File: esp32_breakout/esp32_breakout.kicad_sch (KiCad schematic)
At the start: 25 parts, among them J1 JST B5B-PH-K-S, J10 JST B6B-PH-K-S, J2 JST B5B-PH-K-S, J3 JST B7B-PH-K-S, J4 XT30U-M, J5 HDR M VERT 12p 2.54mm, J9 JST B6B-PH-K-S, SW1 SS12D10, U1 ESP32 DEV KIT Module 30-pin, U2 LM2596 Module

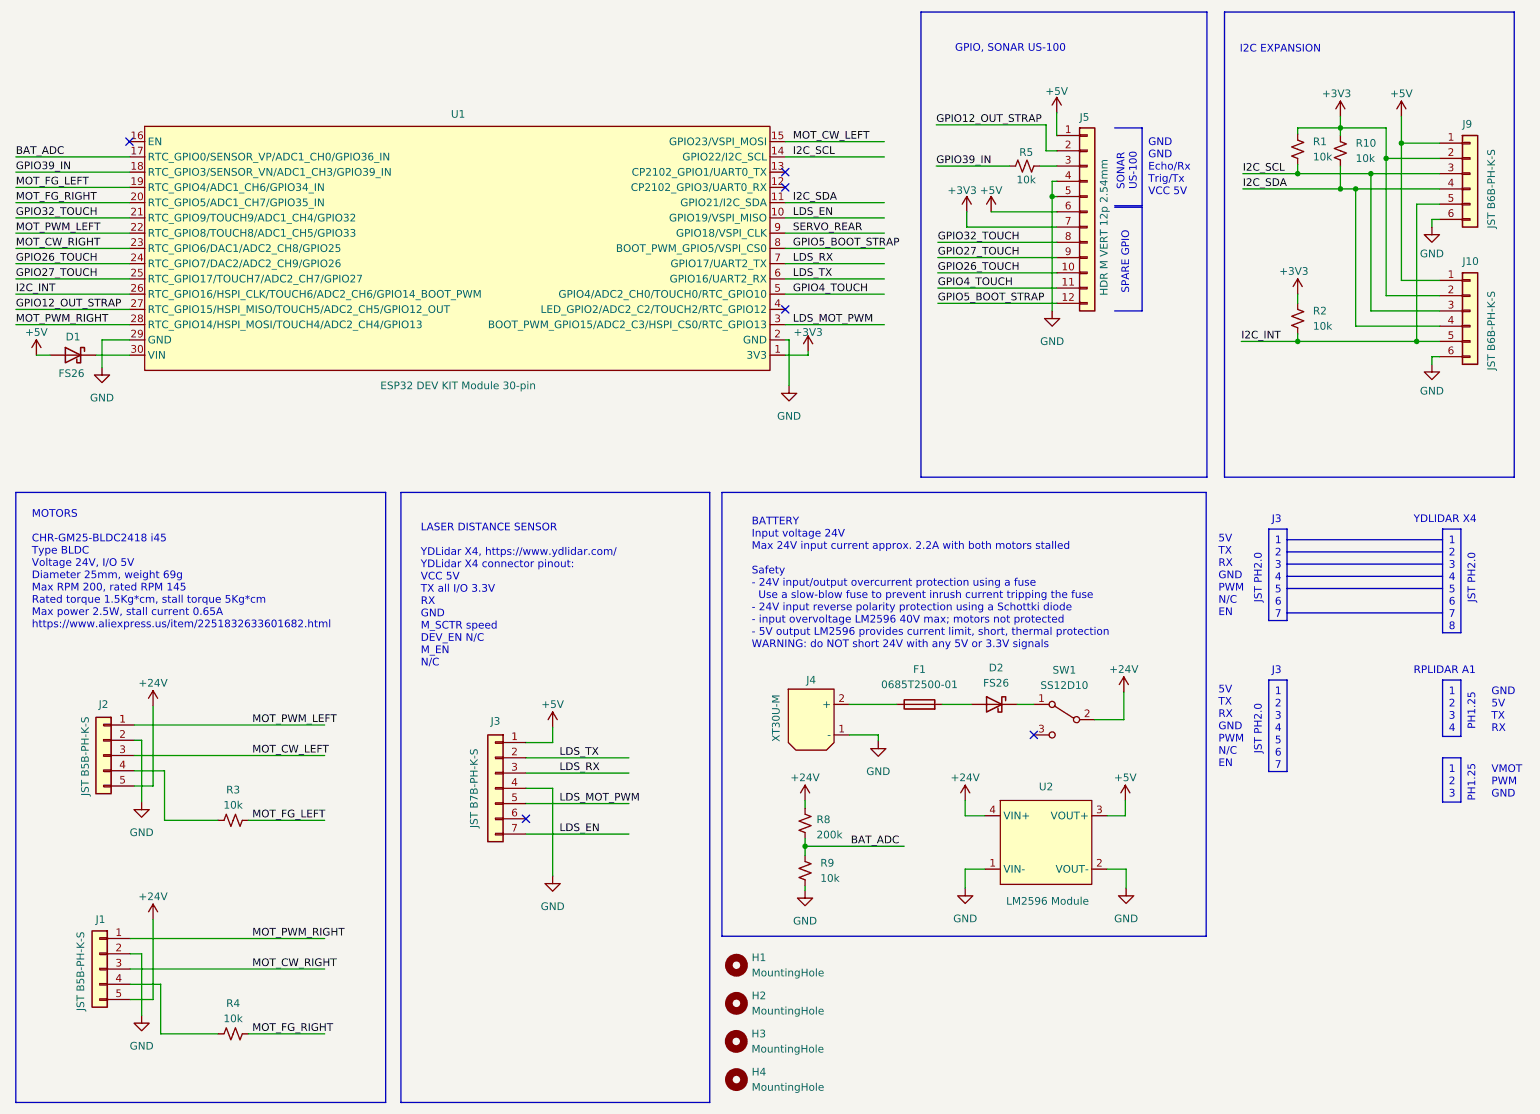
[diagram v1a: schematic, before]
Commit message: ZH extension connector; 6-pin LDS connector
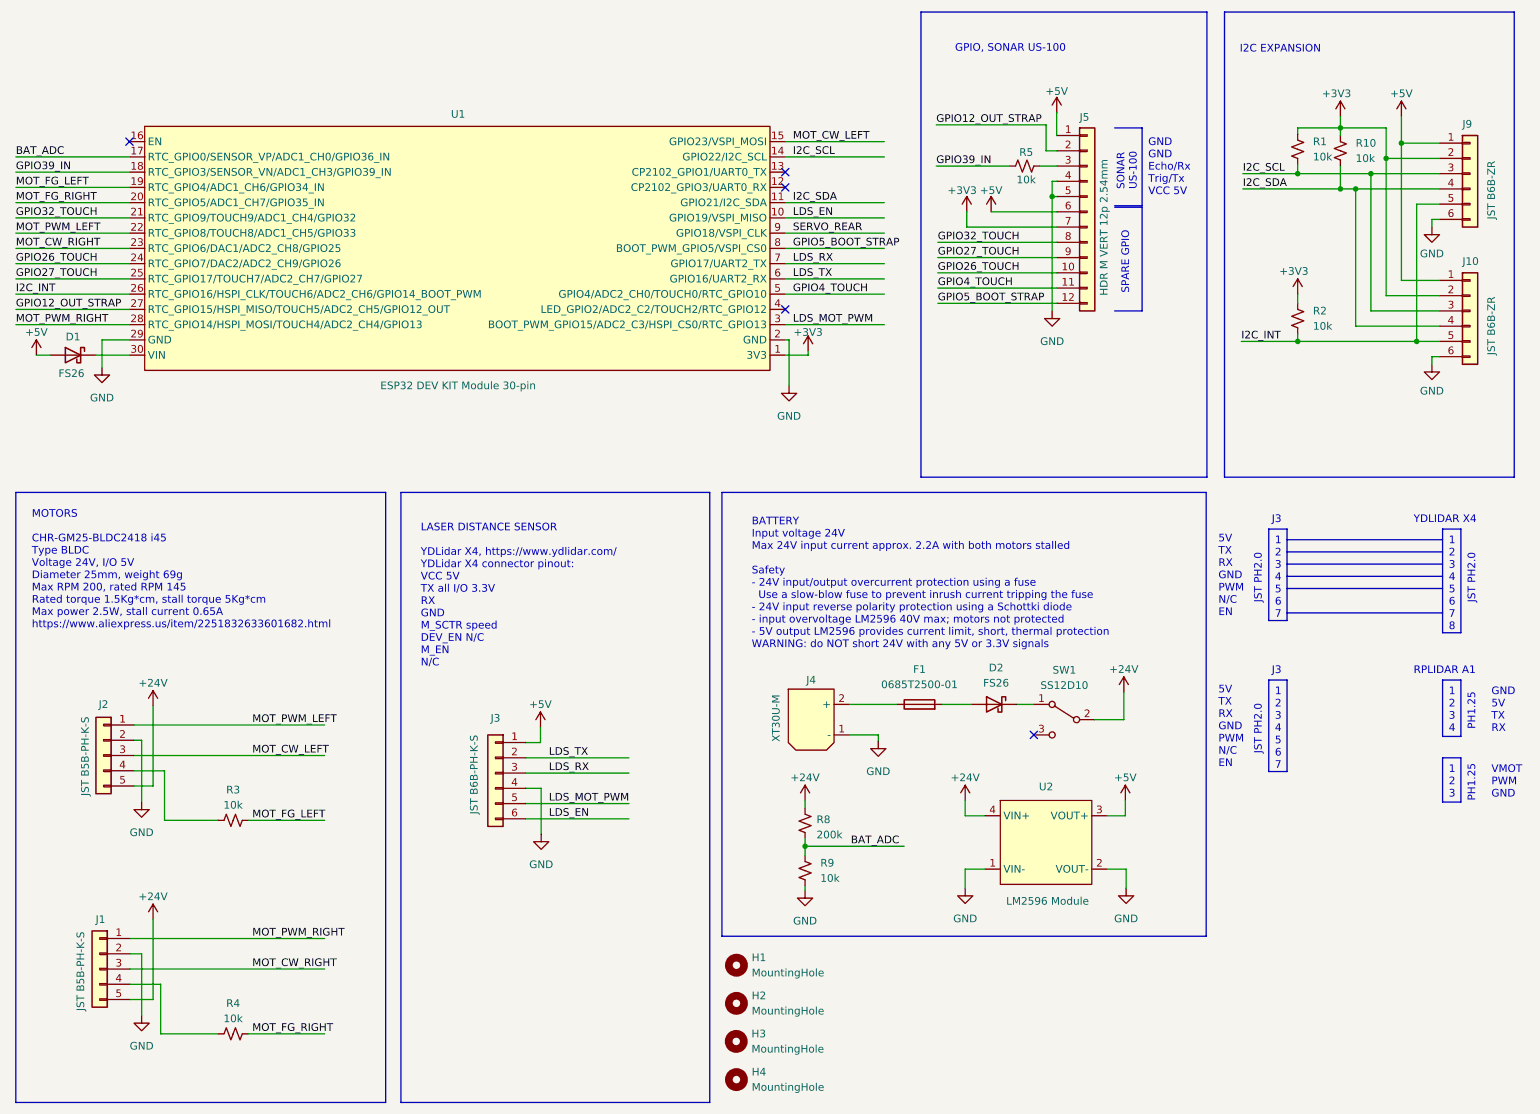
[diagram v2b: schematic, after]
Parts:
- removed J3: JST B7B-PH-K-S, Connector_JST:JST_PH_B7B-PH-K_1x07_P2.00mm_Vertical, symbol Connector_Generic:Conn_01x07
- added J3: JST B6B-PH-K-S, Connector_JST:JST_PH_B6B-PH-K_1x06_P2.00mm_Vertical, symbol Connector_Generic:Conn_01x06
- J10, J9: value JST B6B-PH-K-S -> JST B6B-ZR; footprint Connector_JST:JST_PH_B6B-PH-K_1x06_P2.00mm_Vertical -> Makerspet:JST_ZH_B6B-ZR_1x06_P1.50mm_Vertical
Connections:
- net +5V: now also J3.1 (Pin_1)
- net GND: now also J3.4 (Pin_4)
- net LDS_EN: now also J3.6 (Pin_6)
- net LDS_MOT_PWM: now also J3.5 (Pin_5)
- net LDS_RX: now also J3.3 (Pin_3)
- net LDS_TX: now also J3.2 (Pin_2)
- no-connect marks 6 -> 5
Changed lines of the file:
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@@
   (title_block
     (title "Maker's Pet ESP32 Breakout")
-    (date "2023-12-29")
-    (rev "1.1.0")
+    (date "2024-03-06")
+    (rev "1.2.0")
     (company "Maker's Pet")
     (comment 1 "makerspet.com")
@@
   (no_connect (at 142.748 44.45))
   (no_connect (at 142.748 41.91))
-  (no_connect (at 99.568 149.606))
   (no_connect (at 142.748 64.77))
   (no_connect (at 184.15 135.636))
@@
     (stroke (width 0) (type default))
   )
-  (wire (pts (xy 99.568 136.906) (xy 104.013 136.906))
+  (wire (pts (xy 99.568 136.906) (xy 101.981 136.906))
     (stroke (width 0) (type default))
   )
@@
     (stroke (width 0) (type default))
   )
-  (wire (pts (xy 104.013 134.366) (xy 104.013 136.906))
+  (wire (pts (xy 101.981 134.366) (xy 101.981 136.906))
     (stroke (width 0) (type default))
   )
@@
     (stroke (width 0) (type default))
   )
+  (wire (pts (xy 99.568 149.606) (xy 116.713 149.606))
+    (stroke (width 0) (type default))
+  )
   (wire (pts (xy 14.605 39.37) (xy 33.528 39.37))
     (stroke (width 0) (type default))
@@
     (stroke (width 0) (type default))
   )
-  (wire (pts (xy 99.568 144.526) (xy 104.013 144.526))
+  (wire (pts (xy 99.568 144.526) (xy 102.108 144.526))
     (stroke (width 0) (type default))
   )
@@
     (stroke (width 0) (type default))
   )
-  (wire (pts (xy 104.013 144.526) (xy 104.013 159.131))
+  (wire (pts (xy 102.108 144.526) (xy 102.108 152.146))
     (stroke (width 0) (type default))
   )
@@
   )
   (wire (pts (xy 153.416 130.556) (xy 161.29 130.556))
-    (stroke (width 0) (type default))
-  )
-  (wire (pts (xy 99.568 152.146) (xy 116.713 152.146))
     (stroke (width 0) (type default))
   )
@@
     (effects (font (size 1.27 1.27)) (justify left bottom))
   )
-  (label "LDS_TX" (at 105.156 139.446 0) (fields_autoplaced)
+  (label "LDS_EN" (at 103.378 149.606 0) (fields_autoplaced)
+    (effects (font (size 1.27 1.27)) (justify left bottom))
+  )
+  (label "LDS_TX" (at 103.378 139.446 0) (fields_autoplaced)
     (effects (font (size 1.27 1.27)) (justify left bottom))
   )
@@
     (effects (font (size 1.27 1.27)) (justify left bottom))
   )
-  (label "LDS_MOT_PWM" (at 105.156 147.066 0) (fields_autoplaced)
+  (label "LDS_MOT_PWM" (at 103.378 147.066 0) (fields_autoplaced)
     (effects (font (size 1.27 1.27)) (justify left bottom))
   )
@@
     (effects (font (size 1.27 1.27)) (justify left bottom))
   )
-  (label "LDS_RX" (at 105.156 141.986 0) (fields_autoplaced)
+  (label "LDS_RX" (at 103.378 141.986 0) (fields_autoplaced)
     (effects (font (size 1.27 1.27)) (justify left bottom))
   )
@@
   )
   (label "MOT_PWM_RIGHT" (at 14.605 67.31 0) (fields_autoplaced)
-    (effects (font (size 1.27 1.27)) (justify left bottom))
-  )
-  (label "LDS_EN" (at 105.156 152.146 0) (fields_autoplaced)
     (effects (font (size 1.27 1.27)) (justify left bottom))
   )
@@
       (effects (font (size 1.27 1.27)) (justify left))
     )
-    (property "Value" "JST B6B-PH-K-S" (at 260.35 74.93 90)
+    (property "Value" "JST B6B-ZR" (at 260.35 72.39 90)
       (effects (font (size 1.27 1.27)) (justify left))
     )
-    (property "Footprint" "Connector_JST:JST_PH_B6B-PH-K_1x06_P2.00mm_Vertical" (at 256.794 65.024 0)
+    (property "Footprint" "Makerspet:JST_ZH_B6B-ZR_1x06_P1.50mm_Vertical" (at 256.794 65.024 0)
       (effects (font (size 1.27 1.27)) hide)
     )
@@
         (path "/e24ae185-8f18-408c-aee8-f727519bade3"
           (reference "R1") (unit 1)
-        )
-      )
-    )
-  )
-  (symbol (lib_id "Connector_Generic:Conn_01x07") (at 94.488 144.526 0) (mirror y) (unit 1)
-    (in_bom yes) (on_board yes) (dnp no)
-    (property "Reference" "J3" (at 94.488 133.35 0)
-      (effects (font (size 1.27 1.27)))
-    )
-    (property "Value" "JST B7B-PH-K-S" (at 90.932 144.526 90)
-      (effects (font (size 1.27 1.27)))
-    )
-    (property "Footprint" "Connector_JST:JST_PH_B7B-PH-K_1x07_P2.00mm_Vertical" (at 94.488 144.526 0)
-      (effects (font (size 1.27 1.27)) hide)
-    )
-    (property "Datasheet" "~" (at 94.488 144.526 0)
-      (effects (font (size 1.27 1.27)) hide)
-    )
-    (pin "1")
-    (pin "2")
-    (pin "3")
-    (pin "4")
-    (pin "5")
-    (pin "6")
-    (pin "7")
-    (instances
-      (project "esp32_breakout"
-        (path "/e24ae185-8f18-408c-aee8-f727519bade3"
-          (reference "J3") (unit 1)
         )
       )
@@
     )
   )
-  (symbol (lib_id "power:+5V") (at 104.013 134.366 0) (unit 1)
-    (in_bom yes) (on_board yes) (dnp no) (fields_autoplaced)
-    (property "Reference" "#PWR09" (at 104.013 138.176 0)
-      (effects (font (size 1.27 1.27)) hide)
-    )
-    (property "Value" "+5V" (at 104.013 130.556 0)
-      (effects (font (size 1.27 1.27)))
-    )
-    (property "Footprint" "" (at 104.013 134.366 0)
-      (effects (font (size 1.27 1.27)) hide)
-    )
-    (property "Datasheet" "" (at 104.013 134.366 0)
+  (symbol (lib_id "power:+5V") (at 101.981 134.366 0) (unit 1)
+    (in_bom yes) (on_board yes) (dnp no) (fields_autoplaced)
+    (property "Reference" "#PWR09" (at 101.981 138.176 0)
+      (effects (font (size 1.27 1.27)) hide)
+    )
+    (property "Value" "+5V" (at 101.981 130.556 0)
+      (effects (font (size 1.27 1.27)))
+    )
+    (property "Footprint" "" (at 101.981 134.366 0)
+      (effects (font (size 1.27 1.27)) hide)
+    )
+    (property "Datasheet" "" (at 101.981 134.366 0)
       (effects (font (size 1.27 1.27)) hide)
     )
@@
     )
   )
-  (symbol (lib_id "power:GND") (at 104.013 159.131 0) (unit 1)
-    (in_bom yes) (on_board yes) (dnp no) (fields_autoplaced)
-    (property "Reference" "#PWR010" (at 104.013 165.481 0)
-      (effects (font (size 1.27 1.27)) hide)
-    )
-    (property "Value" "GND" (at 104.013 164.211 0)
-      (effects (font (size 1.27 1.27)))
-    )
-    (property "Footprint" "" (at 104.013 159.131 0)
-      (effects (font (size 1.27 1.27)) hide)
-    )
-    (property "Datasheet" "" (at 104.013 159.131 0)
+  (symbol (lib_id "power:GND") (at 102.108 152.146 0) (unit 1)
+    (in_bom yes) (on_board yes) (dnp no) (fields_autoplaced)
+    (property "Reference" "#PWR010" (at 102.108 158.496 0)
+      (effects (font (size 1.27 1.27)) hide)
+    )
+    (property "Value" "GND" (at 102.108 157.226 0)
+      (effects (font (size 1.27 1.27)))
+    )
+    (property "Footprint" "" (at 102.108 152.146 0)
+      (effects (font (size 1.27 1.27)) hide)
+    )
+    (property "Datasheet" "" (at 102.108 152.146 0)
       (effects (font (size 1.27 1.27)) hide)
     )
@@
     )
   )
+  (symbol (lib_id "Connector_Generic:Conn_01x06") (at 94.488 141.986 0) (mirror y) (unit 1)
+    (in_bom yes) (on_board yes) (dnp no)
+    (property "Reference" "J3" (at 94.488 132.842 0)
+      (effects (font (size 1.27 1.27)))
+    )
+    (property "Value" "JST B6B-PH-K-S" (at 90.932 142.24 90)
+      (effects (font (size 1.27 1.27)))
+    )
+    (property "Footprint" "Connector_JST:JST_PH_B6B-PH-K_1x06_P2.00mm_Vertical" (at 94.488 141.986 0)
+      (effects (font (size 1.27 1.27)) hide)
+    )
+    (property "Datasheet" "~" (at 94.488 141.986 0)
+      (effects (font (size 1.27 1.27)) hide)
+    )
+    (pin "1")
+    (pin "6")
+    (pin "4")
+    (pin "2")
+    (pin "3")
+    (pin "5")
+    (instances
+      (project "esp32_breakout"
+        (path "/e24ae185-8f18-408c-aee8-f727519bade3"
+          (reference "J3") (unit 1)
+        )
+      )
+    )
+  )
   (symbol (lib_id "Device:R_Small_US") (at 182.626 40.894 90) (unit 1)
     (in_bom yes) (on_board yes) (dnp no)
@@
       (effects (font (size 1.27 1.27)) (justify left))
     )
-    (property "Value" "JST B6B-PH-K-S" (at 260.35 51.308 90)
+    (property "Value" "JST B6B-ZR" (at 260.35 49.784 90)
       (effects (font (size 1.27 1.27)) (justify left))
     )
-    (property "Footprint" "Connector_JST:JST_PH_B6B-PH-K_1x06_P2.00mm_Vertical" (at 256.794 42.164 0)
-      (effects (font (size 1.27 1.27)) hide)
-    )
+    (property "Footprint" "Makerspet:JST_ZH_B6B-ZR_1x06_P1.50mm_Vertical" (at 256.794 42.164 0)
+      (effects (font (size 1.27 1.27)) hide)
+    )

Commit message: 12V motors
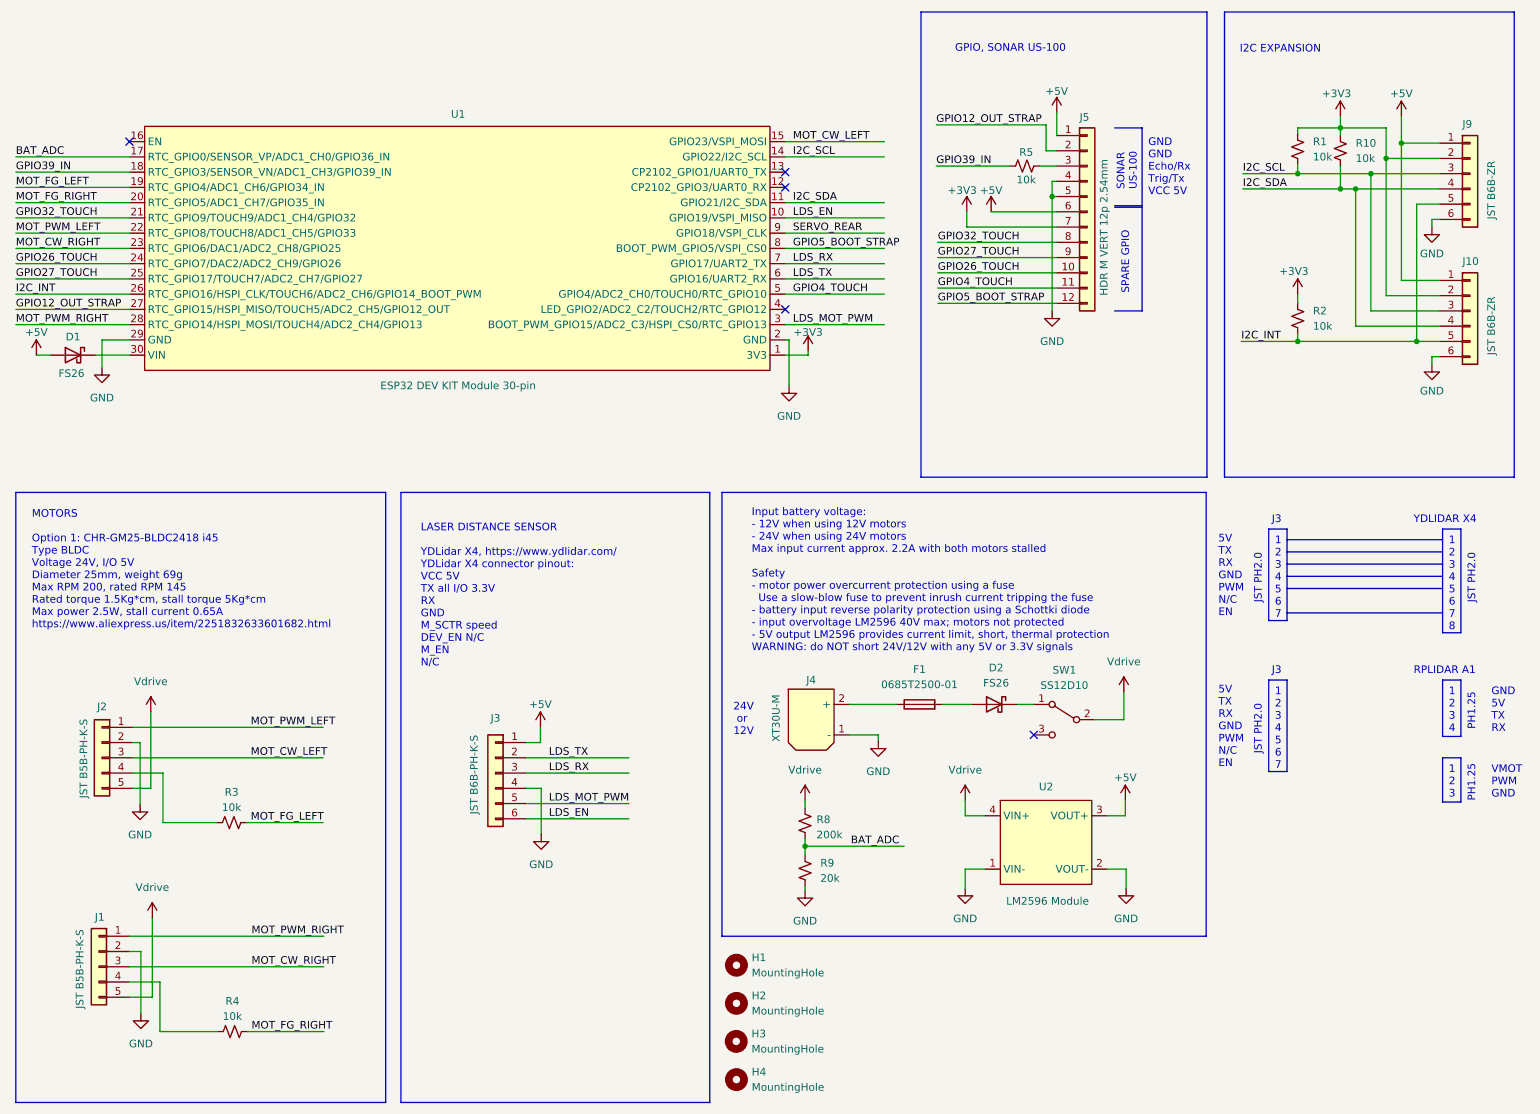
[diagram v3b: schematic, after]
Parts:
- R9: value 10k -> 20k
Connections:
- net +24V renamed Vdrive
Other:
- note added: "24V or 12V"
- note added: "Input battery voltage: - 12V when using 12V motors - 24V when using 24V motors Max input current approx. 2.2A with both motors stalled Safety - motor power overcurrent protection using a fuse Use a slow-blow fuse to prevent inrush current tripping the fuse - battery input reverse polarity protection using a Schottki diode - input overvoltage LM2596 40V max; motors not protected - 5V output LM2596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"
- note added: "MOTORS Option 1: CHR-GM25-BLDC2418 i45 Type BLDC Voltage 24V, I/O 5V Diameter 25mm, weight 69g Max RPM 200, rated RPM 145 Rated torque 1.5Kg*cm, stall torque 5Kg*cm Max power 2.5W, stall current 0.65A https://www.aliexpress.us/item/2251832633601682.html"
- note removed: "BATTERY Input voltage 24V Max 24V input current approx. 2.2A with both motors stalled Safety - 24V input/output overcurrent protection using a fuse Use a slow-blow fuse to prevent inrush current tripping the fuse - 24V input reverse polarity protection using a Schottki diode - input overvoltage LM2596 40V max; motors not protected - 5V output LM2596 provides current limit, short, thermal protecti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"
- note removed: "MOTORS CHR-GM25-BLDC2418 i45 Type BLDC Voltage 24V, I/O 5V Diameter 25mm, weight 69g Max RPM 200, rated RPM 145 Rated torque 1.5Kg*cm, stall torque 5Kg*cm Max power 2.5W, stall current 0.65A https://www.aliexpress.us/item/2251832633601682.html"
- company: Maker's Pet -> makerspet.com
- title: Maker's Pet ESP32 Breakout -> ESP32 Breakout
